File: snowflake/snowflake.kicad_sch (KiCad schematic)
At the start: 73 parts, among them J3 TC2030, SW1 SK-12E12-G040, U1 TZ-5050S2RGB-5V-I4-H1, U10 TZ-5050S2RGB-5V-I4-H1, U11 TZ-5050S2RGB-5V-I4-H1, U12 TZ-5050S2RGB-5V-I4-H1, U13 TZ-5050S2RGB-5V-I4-H1, U14 TZ-5050S2RGB-5V-I4-H1, U15 TZ-5050S2RGB-5V-I4-H1, U16 TZ-5050S2RGB-5V-I4-H1, U17 TZ-5050S2RGB-5V-I4-H1, U18 TZ-5050S2RGB-5V-I4-H1, U19 TZ-5050S2RGB-5V-I4-H1, U2 TZ-5050S2RGB-5V-I4-H1, U20 TZ-5050S2RGB-5V-I4-H1, U21 TZ-5050S2RGB-5V-I4-H1, U22 TZ-5050S2RGB-5V-I4-H1, U23 TZ-5050S2RGB-5V-I4-H1, U24 TZ-5050S2RGB-5V-I4-H1, U25 TPS61022, U26 CH32V003F4U6, U3 TZ-5050S2RGB-5V-I4-H1, U4 TZ-5050S2RGB-5V-I4-H1, U5 TZ-5050S2RGB-5V-I4-H1, U6 TZ-5050S2RGB-5V-I4-H1, U7 TZ-5050S2RGB-5V-I4-H1, U8 TZ-5050S2RGB-5V-I4-H1, U9 TZ-5050S2RGB-5V-I4-H1

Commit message: First prototype
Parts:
- removed C66: 100n, Capacitor_SMD:C_0402_1005Metric, symbol Device:C_Small
- C66: renamed from C65; value 100n -> 100nF; symbol Device:C_Small -> Device:C
- R3: value GT36516 -> C2904881; symbol easyeda2kicad:GT36516 -> easyeda2kicad:GT36528; LCSC Part C2904880 -> C2904881
- U1, U10, U11, U12, U13, U14, U15, U16, U17, U18, U19, U2, U20, U21, U22, U23, U24, U3, U4, U5, U6, U7, U8, U9: LCSC Part (none) -> C26167850
- U25: footprint Package_DFN_QFN:Texas_RWU0007A_VQFN-7_2x2mm_P0.5mm -> easyeda2kicad:VQFN-7_L2.0-W2.0-P0.55-TL_RWU; symbol Converter_DCDC:TPS61022 -> easyeda2kicad:TPS61022RWUR; LCSC Part (none) -> C915088
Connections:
- net TOUCH1: now also U26.16 (PD2/A3); no longer U26.18 (PD4/A7)
- net TOUCH3: now also U26.18 (PD4/A7); no longer U26.16 (PD2/A3)
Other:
- moved on the sheet: C25, C26, C27, L1, R1, R2

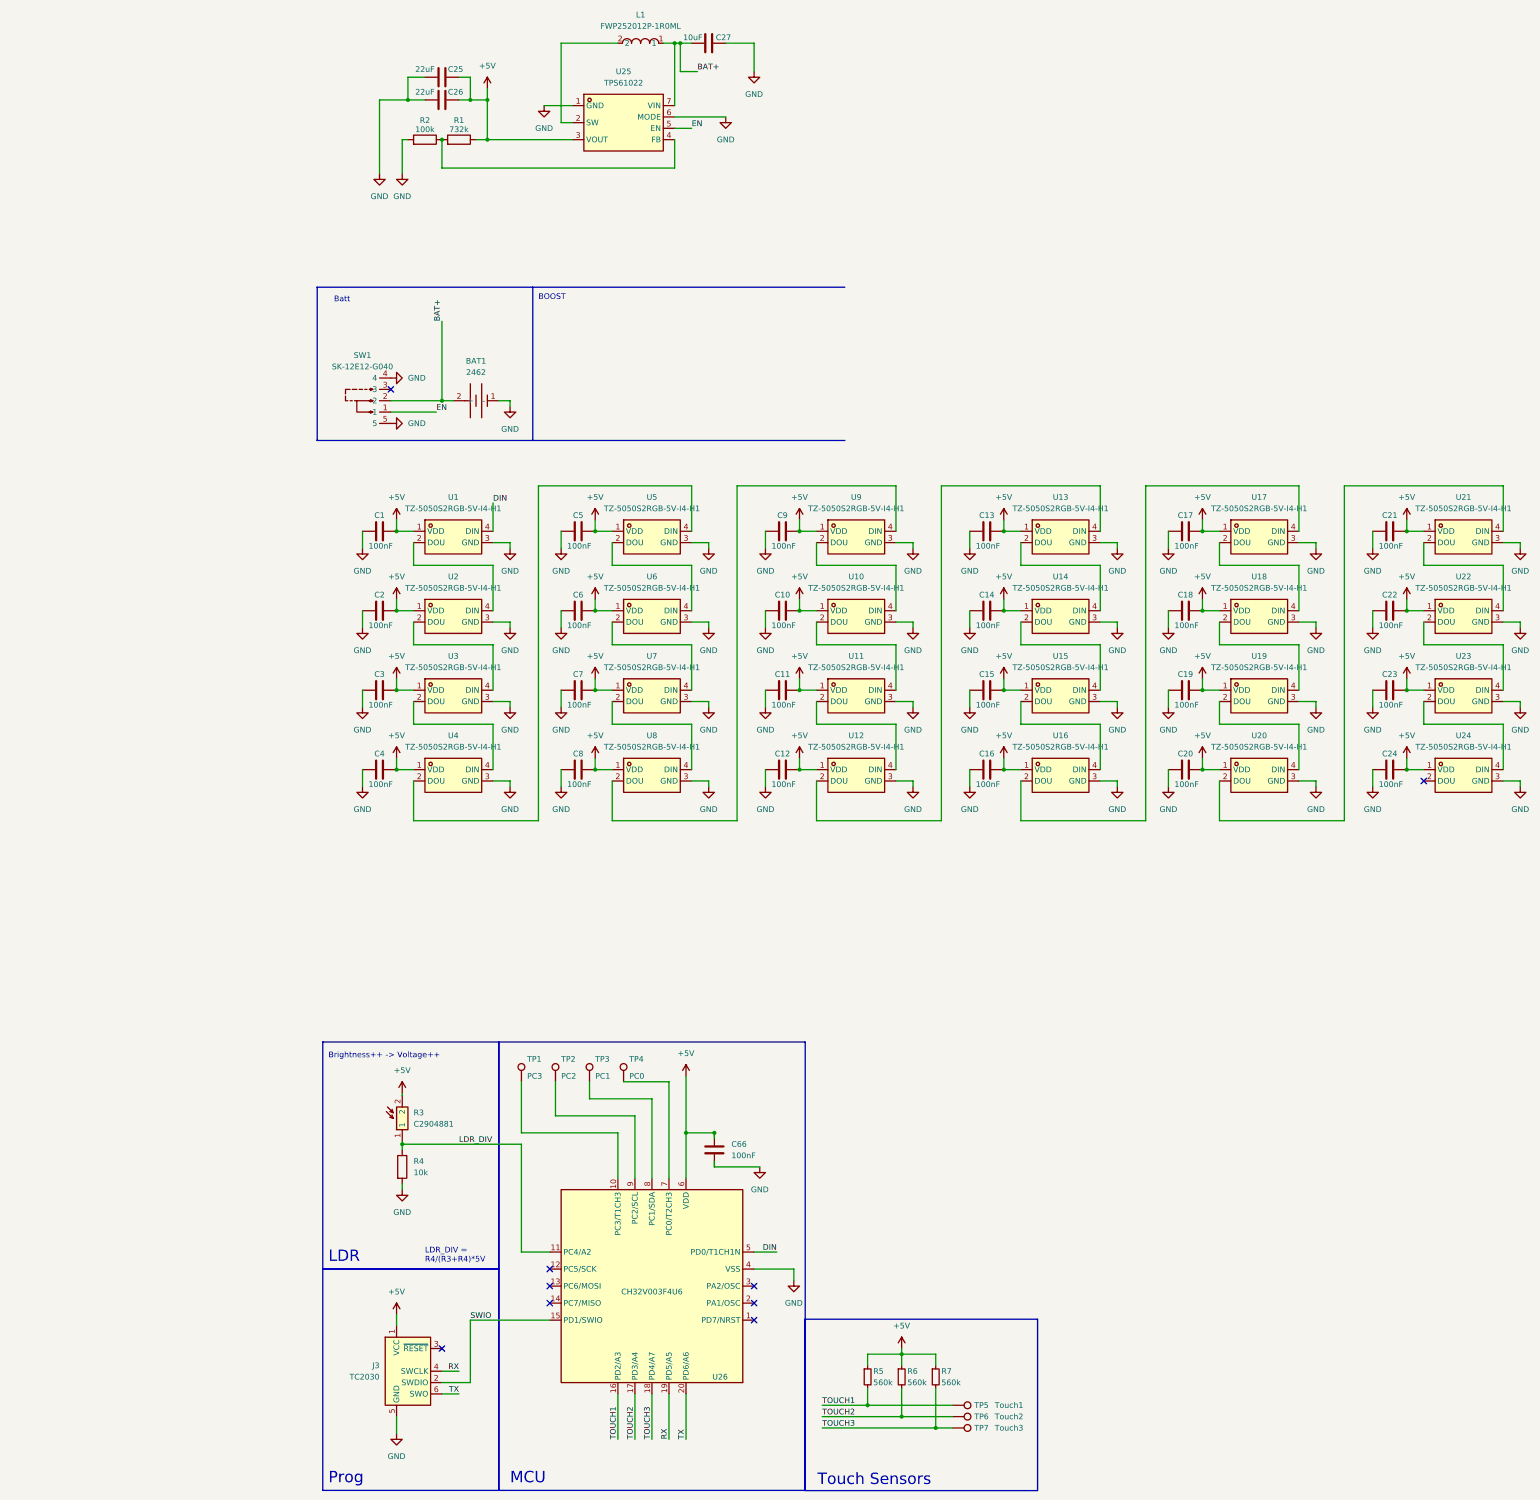
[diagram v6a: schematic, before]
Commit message: Use basic parts, fix boost converter positioning
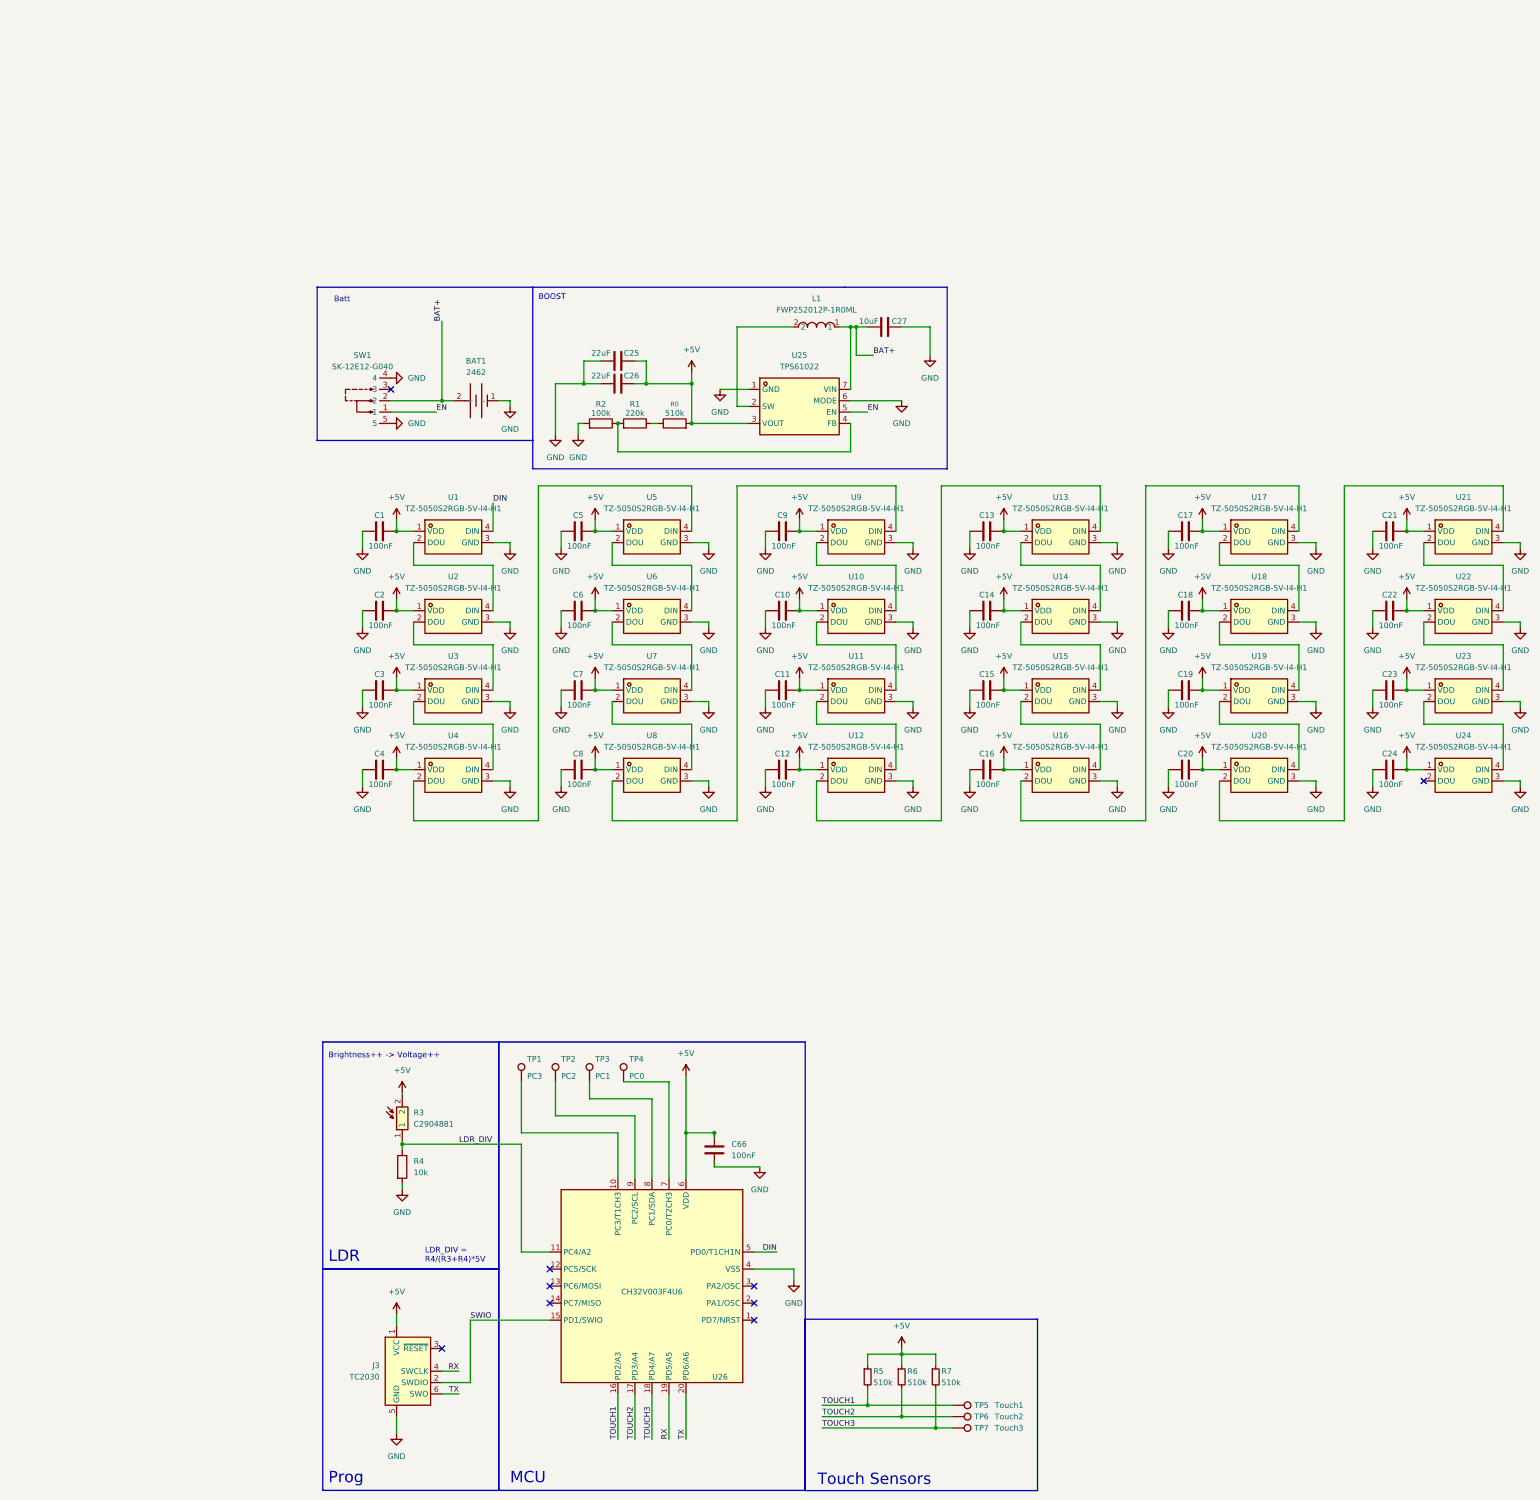
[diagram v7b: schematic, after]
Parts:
- added R0: 510k, Resistor_SMD:R_0603_1608Metric, symbol Device:R
- BAT1: LCSC (none) -> C3029547; now left out of the parts list
- C1, C10, C11, C12, C13, C14, C15, C16, C17, C18, C19, C2, C20, C21, C22, C23, C24, C3, C4, C5, C6, C7, C8, C9: LCSC C36911391 -> C14663
- C25, C26: LCSC C20416425 -> C59461
- C27: LCSC C6119842 -> C19702
- R1: value 732k -> 220k; footprint Resistor_SMD:R_0402_1005Metric -> Resistor_SMD:R_0603_1608Metric; LCSC C5159692 -> C22961
- R2: LCSC C49652939 -> C25741
- R3: LCSC (none) -> C2904881
- R5, R6, R7: value 560k -> 510k; LCSC C23203 -> C23192
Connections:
- net +5V: now also R0.2; no longer R1.1
- new net: R0.1, R1.1
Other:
- moved on the sheet: C25, C26, C27, L1, R1, R2, U25

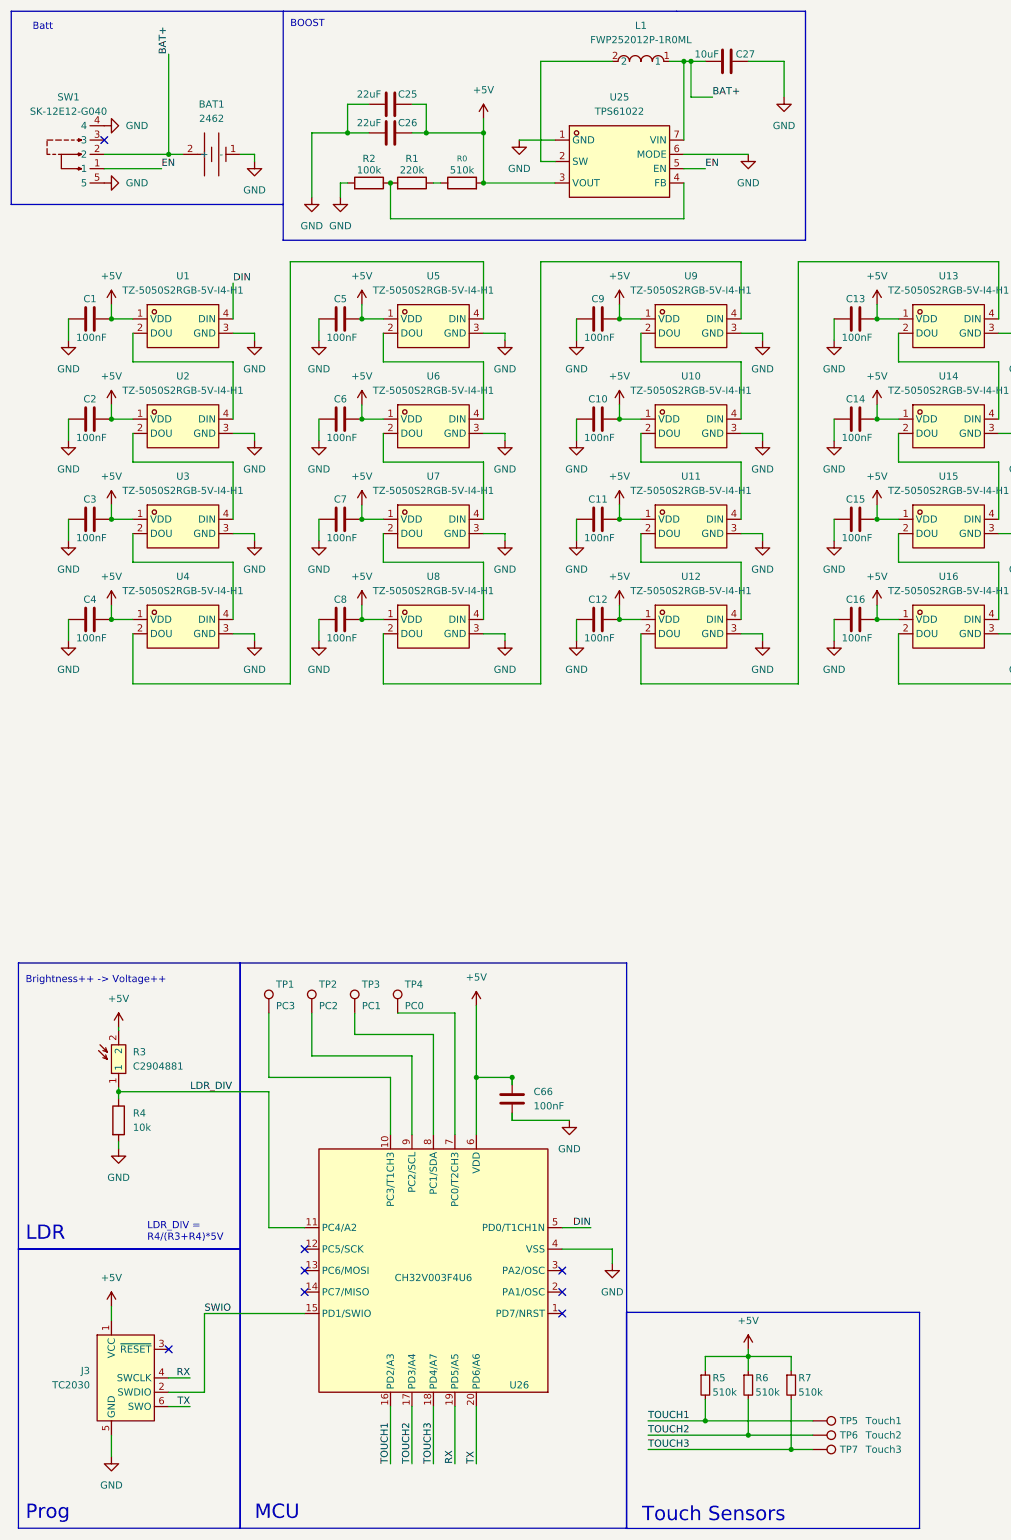
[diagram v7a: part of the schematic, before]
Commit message: put everything on one side
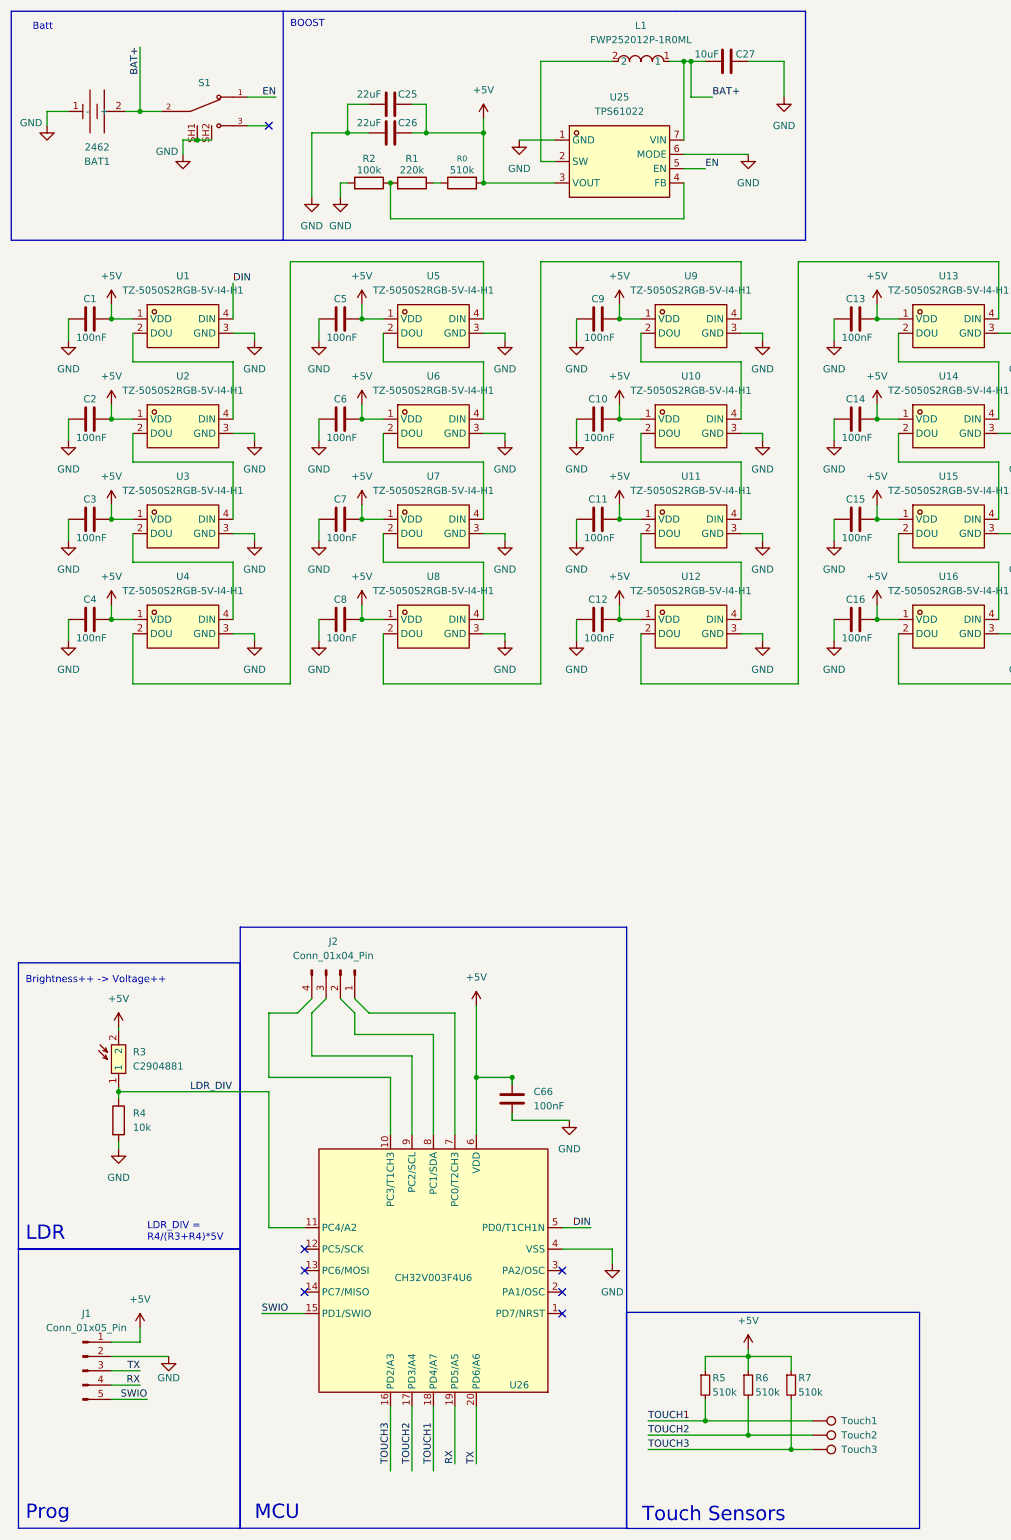
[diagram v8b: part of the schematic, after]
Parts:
- removed J3: TC2030, Connector:Tag-Connect_TC2030-IDC-NL_2x03_P1.27mm_Vertical, symbol Connector:Conn_ARM_SWD_TagConnect_TC2030-NL
- removed SW1: SK-12E12-G040, easyeda2kicad:SW-TH_SK-12E12-G040, symbol easyeda2kicad:SK-12E12-G040
- removed TP1: PC3, TestPoint:TestPoint_Pad_D2.0mm, symbol Connector:TestPoint
- removed TP2: PC2, TestPoint:TestPoint_Pad_D2.0mm, symbol Connector:TestPoint
- removed TP3: PC1, TestPoint:TestPoint_Pad_D2.0mm, symbol Connector:TestPoint
- removed TP4: PC0, TestPoint:TestPoint_Pad_D2.0mm, symbol Connector:TestPoint
- added J1: Conn_01x05_Pin, Connector_PinHeader_2.54mm:PinHeader_1x05_P2.54mm_Vertical, symbol Connector:Conn_01x05_Pin
- added J2: Conn_01x04_Pin, Connector_PinHeader_2.54mm:PinHeader_1x04_P2.54mm_Vertical, symbol Connector:Conn_01x04_Pin
- added S1: SLW-1277545-3A-RA-N-D, Digikey:SW_SLW-1277545-3A-RA-N-D, symbol Digikey:SLW-1277545-3A-RA-N-D
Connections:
- net +5V: now also J1.1 (Pin_1)
- net BAT+: now also S1.2
- net EN: now also S1.1
- net GND: now also J1.2 (Pin_2), S1.SH1, S1.SH2
- net RX: now also J1.4 (Pin_4)
- net SWIO: now also J1.5 (Pin_5)
- net TOUCH1: now also U26.18 (PD4/A7); no longer U26.16 (PD2/A3)
- net TOUCH3: now also U26.16 (PD2/A3); no longer U26.18 (PD4/A7)
- net TX: now also J1.3 (Pin_3)
- net at U26.9 (PC2/SCL): now also J2.3 (Pin_3)
- net at U26.10 (PC3/T1CH3): now also J2.4 (Pin_4)
- net at U26.7 (PC0/T2CH3): now also J2.1 (Pin_1)
- net at U26.8 (PC1/SDA): now also J2.2 (Pin_2)
- no-connect marks 9 -> 8
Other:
- moved on the sheet: BAT1
